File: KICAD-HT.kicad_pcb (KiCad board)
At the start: 4 copper layers, 85 x 70 mm, 147 parts, among them J1 HV_BIAS_IN, J2 DC_HT, Q1 IPD050N10N5, Q2 IPD050N10N5, Q4 MMBF170, Q5 IPD60R360P7, Q6 BSS127I, Q7 BSS127I, T1 MSD1514-103ME, U1 UCC27517, U10 ISO7710, U11 AMC0311R, U12 UCC24612, U13 SN74LVC1G08, U14 TSV791, U15 ATL431, U16 LMV7219, U17 SN74LVC1G132, U18 SN74LVC1G74, U19 ISO7710F, U20 VODA1275, U21 MCP6001, U22 AMC0302R, U3 ISO7710, U5 DPC817, U7 AMC0311R, U9 AMC0302R

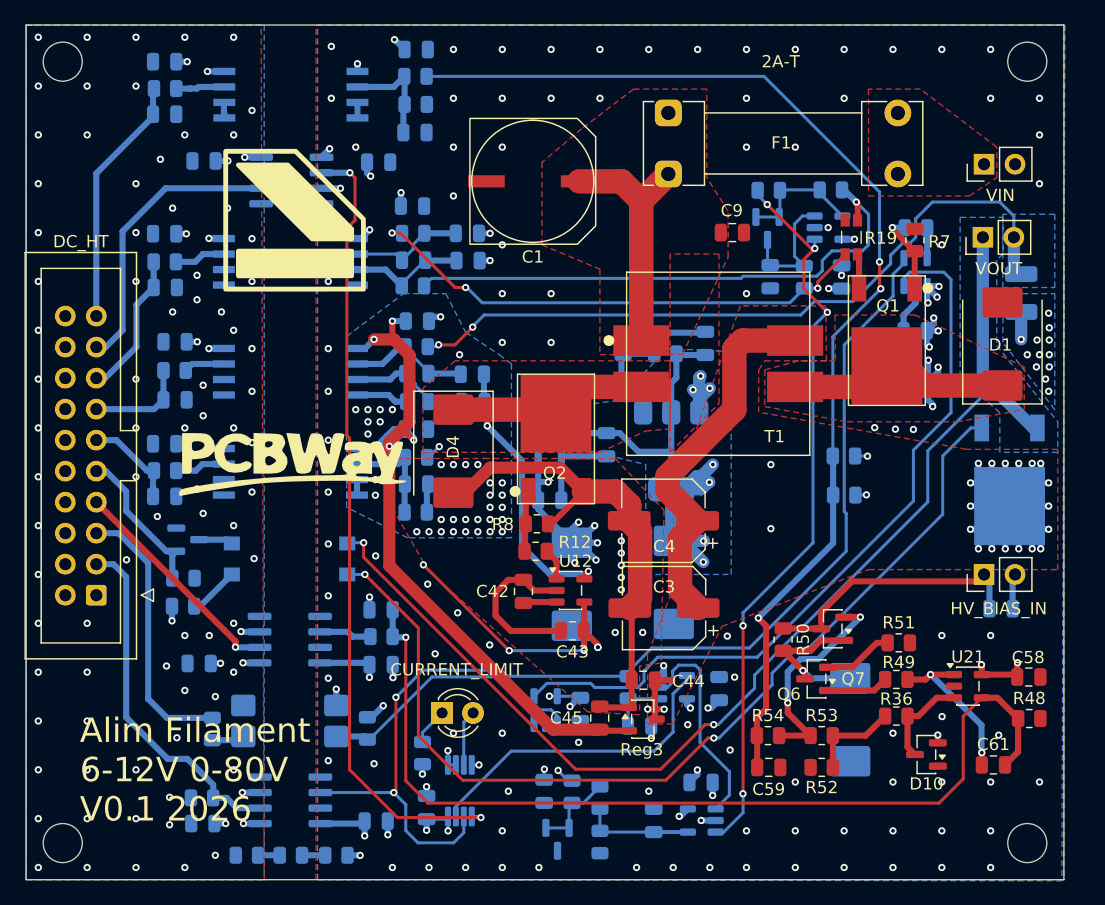
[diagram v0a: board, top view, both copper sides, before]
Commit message: Nettoie les 3 dernieres violations hors silkscreen : exclut les broches NC de barriere_controle (U19 pin7), force la connexion solide aux pastilles GND/VOUT_N starved_thermal (C18/U14/C55/C51)
Co-Authored-By: Claude Sonnet 5 <noreply@anthropic.com>
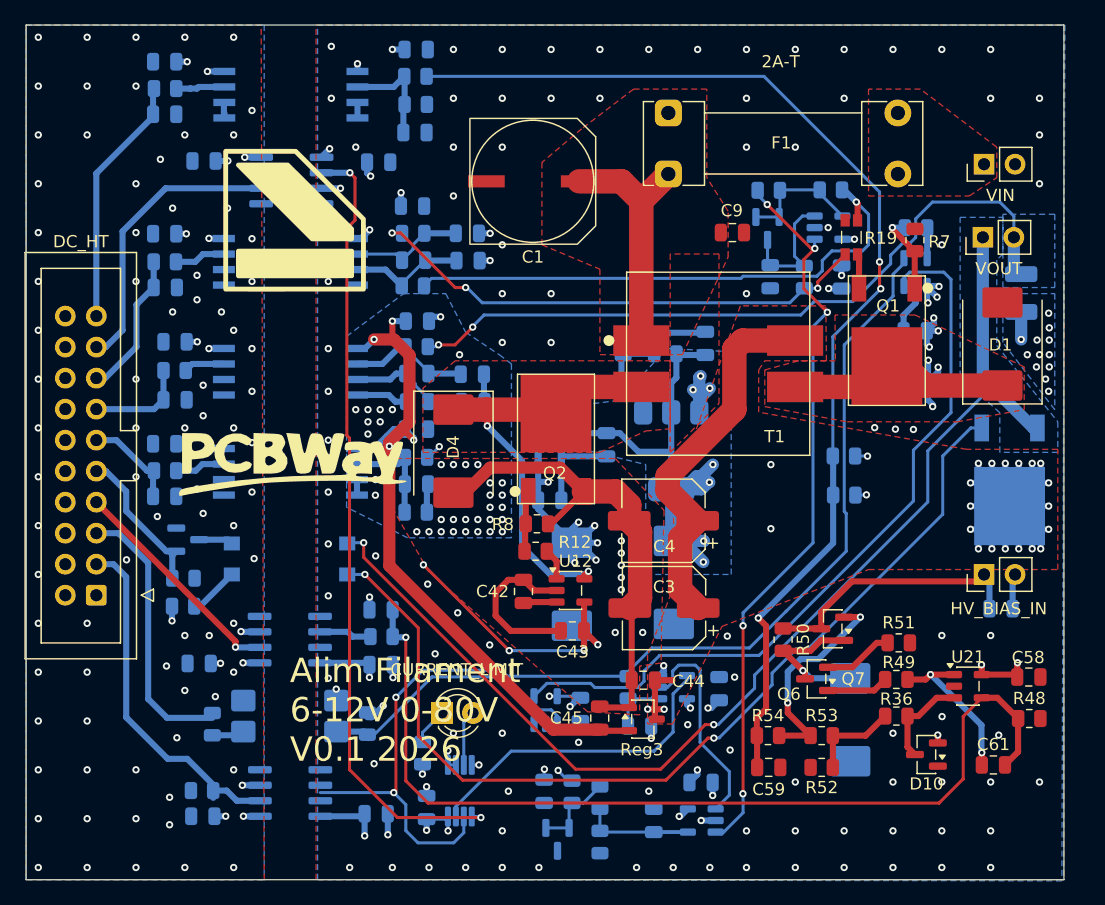
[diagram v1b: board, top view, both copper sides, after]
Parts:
- removed R37, R38, R39: 1M, Resistor_SMD:R_0805_2012Metric
- removed REF** (x4): MountingHole_3.2mm_M3, MountingHole:MountingHole_3.2mm_M3
- moved C15 0.60 mm to (109.5, 111.8)
- moved C16 0.60 mm to (123.7, 111.6)
- moved R5 0.60 mm to (109.4, 109.7)
- moved U3 0.60 mm to (116.6, 109.9)
- moved U5 0.40 mm to (116.6, 103.6)
- moved R3 0.40 mm to (110.3, 104.3)
- moved R4 0.40 mm to (123.0, 104.2)
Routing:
- net Net-(R38-Pad1): track 1.90 -> 0.00 mm
- net Net-(R37-Pad1): track 1.78 -> 0.00 mm
- net GND: track 43.3 -> 42.3 mm, vias 114 -> 113
- net VOUT_P: track 84.6 -> 84.4 mm, vias 27 -> 26

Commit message: Corrige silk_over_copper Q1/Q2/Q5/T1/C1 et ajoute VODA1275 a fp-lib-table
Repercute dans les empreintes placees (copies embarquees du .kicad_pcb)
la correction de contour apportee a TO252-3_TabPin2/MSD1514/A786MW_VChip
dans lib_fp_commun -- KiCad ne resynchronise pas automatiquement une
empreinte placee quand le fichier librairie change, il fallait editer
les deux. Ajoute aussi l'entree VODA1275 manquante dans fp-lib-table
(bibliotheque presente sur disque et deja utilisee par U20, jamais
enregistree ici -- presente dans KICAD-HV, oubliee ici).

41 -> 23 avertissements DRC (0 regression verifiee par diff avant/apres).

Co-Authored-By: Claude Sonnet 5 <noreply@anthropic.com>
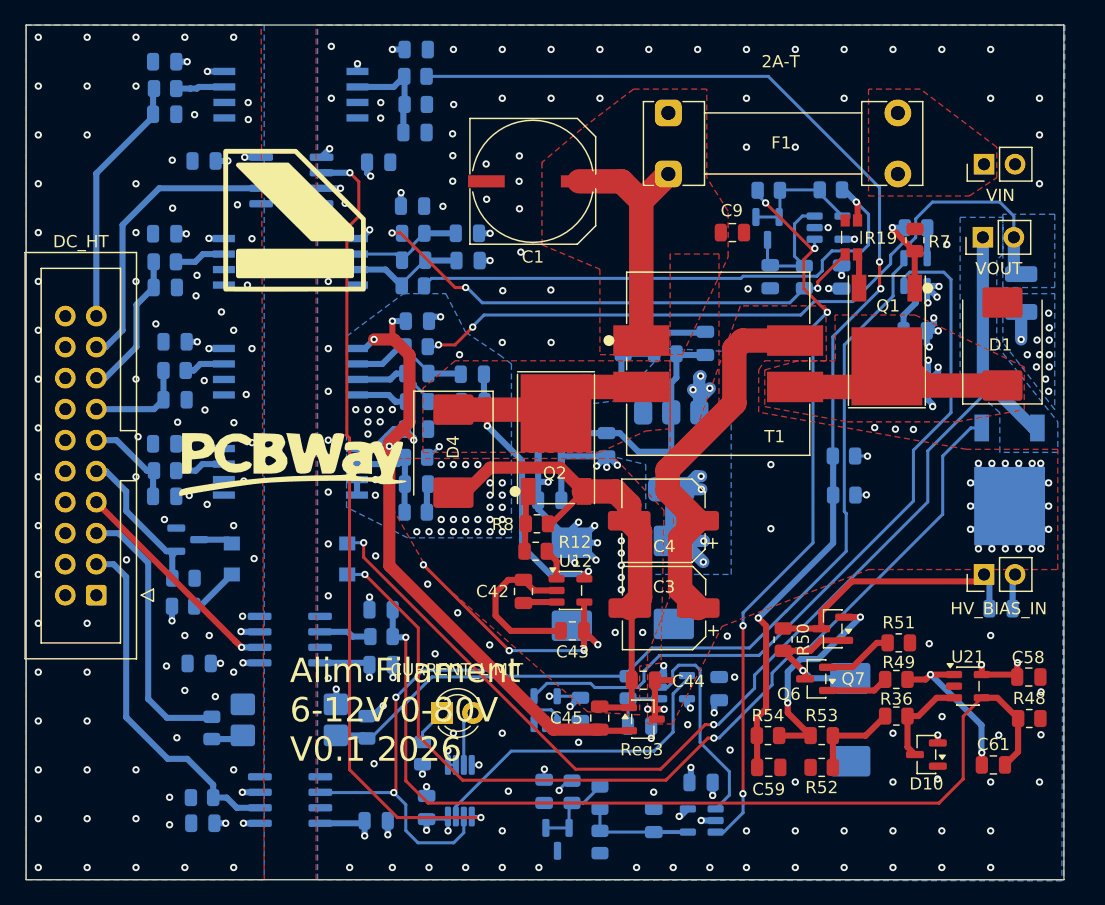
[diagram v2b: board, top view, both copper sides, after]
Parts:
- moved C15 0.58 mm to (109.5, 112.4)
- moved C16 0.58 mm to (123.7, 112.2)
- moved R5 0.58 mm to (109.4, 110.3)
- moved U3 0.57 mm to (116.6, 110.5)
- moved R3 0.31 mm to (110.2, 104.6)
- moved U5 0.31 mm to (116.6, 103.9)
- moved R4 0.31 mm to (122.9, 104.5)
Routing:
- net RAIL_8V25: track 55.1 -> 52.9 mm
- net GND: track 42.3 -> 44.2 mm, vias 113 -> 126
- net GND_CTRL: track 1.30 -> 0.00 mm

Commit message: Corrige le sliver VOUT_N/GND, remet les trous de fixation, fixe le 3D de F1
Travail de nettoyage silkscreen (texte titre, champs reference, J2) et
contour de zone (pointe de cuivre VOUT_N pres du via RAIL_8V25, decouverte
via reconstruction geometrique des zones remplies faute de coordonnees
dans le rapport DRC). Modele 3D de F1 repointe vers
Fuseholder_Cylinder-5x20mm_Schurter_0031_8201_Horizontal_Open.step
(echelle 0.836 pour coller au pas 18.8mm existant) -- le fichier original
Littelfuse_111_Lateral n'a jamais existe dans la bibliotheque 3D KiCad
stock (verifie sur le depot officiel), aucune pastille ni routage touche.

DRC propre (0 violation).

Co-Authored-By: Claude Sonnet 5 <noreply@anthropic.com>
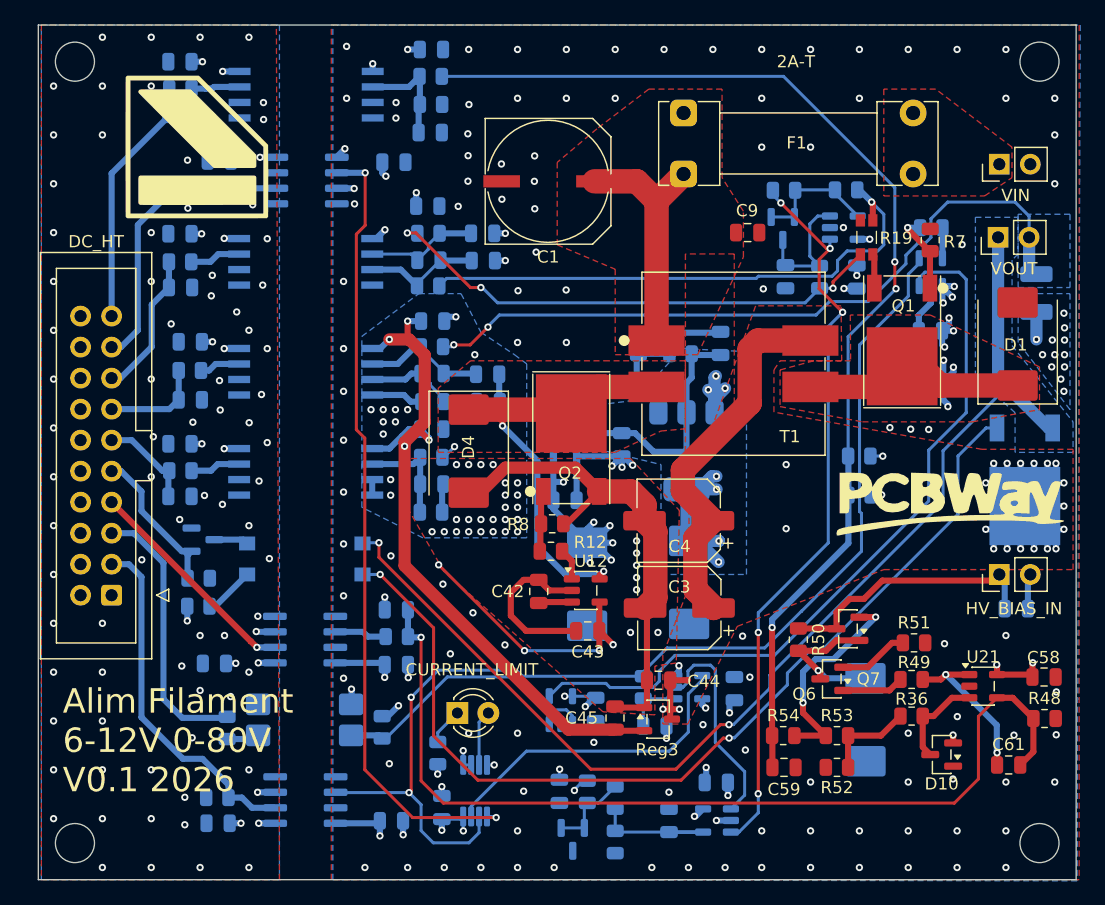
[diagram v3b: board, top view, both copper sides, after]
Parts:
- added H1: MountingScrew, MountingHole:MountingHole_3.2mm_M3, F.Cu at (99.0, 50.0)
- added H2: MountingScrew, MountingHole:MountingHole_3.2mm_M3, F.Cu at (99.0, 114.0)
- added H3: MountingScrew, MountingHole:MountingHole_3.2mm_M3, F.Cu at (178.0, 114.0)
- added H4: MountingScrew, MountingHole:MountingHole_3.2mm_M3, F.Cu at (178.0, 50.0)
- moved G*** 53.9 mm to (171.0, 86.0)
- moved G*** 10.0 mm to (109.0, 57.0)
- moved C37 1.25 mm to (128.3, 71.2)
- moved R40 1.25 mm to (128.2, 73.3)
- moved C1 1.25 mm to (137.8, 59.8)
- moved C10 1.25 mm to (151.9, 73.1)
- moved C13 1.25 mm to (143.8, 81.4)
- moved C14 1.25 mm to (139.1, 85.9)
- moved C15 1.25 mm to (110.7, 112.4)
- moved C16 1.25 mm to (124.9, 112.2)
- moved C18 1.25 mm to (128.2, 80.1)
- moved C19 1.25 mm to (169.1, 72.0)
- moved C21 1.25 mm to (169.2, 76.2)
- moved C23 1.25 mm to (128.2, 84.6)
- moved C24 1.25 mm to (107.6, 85.6)
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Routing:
- net HV_BIAS_OUT: track 93.2 -> 92.6 mm
- net GND_CTRL: vias 80 -> 78

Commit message: Finalise la regle HT_distance_90V (HV_BIAS_OUT trace, starved_thermal C37)
Passes successives de reduction des faux positifs par tracage reel du
circuit (pas par le nom des nets) :
- HV_BIAS_OUT ajoute cote A (pas exclu) : verifie pilote activement par
  la boucle de linearisation (Q7/MCP6001) et couple a VOUT_P/VOUT_N par
  le pont 2x100kOhm R9/R10 -- atteint reellement ~90V, contrairement a
  l'hypothese initiale qui l'avait classe "meme domaine, sans danger".
- HV_BIAS_IN (J1) verifie et laisse hors de la classe SEC : decouple
  vers le vrai GND (C62, J1 broche 2), entree brute avant regulation,
  domaine different malgre le nom proche de HV_BIAS_OUT.
- Net-(U22-INP)/Net-(U22-INN)/ISNS_P ajoutes a la netclasse SEC
  (KICAD-HT.kicad_pro) : U22 (AMC0302R) a sa broche GND1 litteralement
  sur VOUT_N, ISNS_P relie a Net-(U22-INP) via R40 -- meme domaine.
- Exemptions nominative R9, R10, R54 (pastille-contre-pastille-du-
  meme-composant, zone au lieu de pad -- meme motif que T1, cas que
  A.Parent ne couvre pas pour une zone).

DRC propre : 0 violation, 0 element non connecte. Inclut aussi la
correction starved_thermal de C37 (connexion directe a la zone VOUT_N,
pastille trop petite pour 2 rayons de frein thermique).

Co-Authored-By: Claude Sonnet 5 <noreply@anthropic.com>
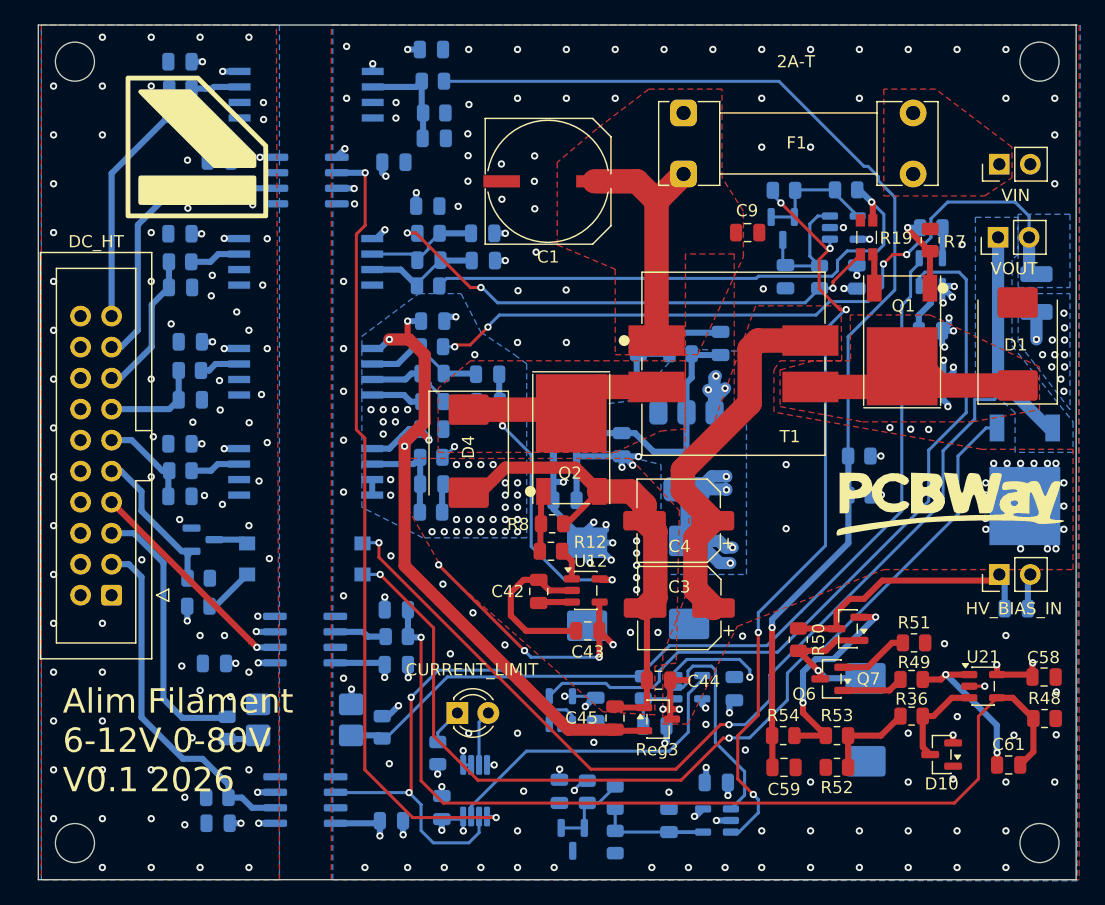
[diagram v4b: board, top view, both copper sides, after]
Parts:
- moved R23 0.74 mm to (128.4, 54.2)
- moved C40 0.58 mm to (128.4, 56.3)
- moved R22 0.43 mm to (128.3, 51.6)
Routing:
- net GND: track 44.2 -> 53.1 mm, vias 126 -> 125
- net VOUT_P: track 84.4 -> 91.3 mm, vias 26 -> 25
- net RAIL_8V25: track 52.9 -> 56.9 mm
- net ISNS_AMP: track 60.8 -> 62.8 mm
- net V_HT_OUT: track 95.7 -> 97.2 mm
- net SW_SEC: track 36.0 -> 37.4 mm
- net ISNS_P: track 62.5 -> 63.4 mm, vias 2 -> 4
- net U15_OUTP: track 79.4 -> 80.2 mm
- net HV_BIAS_OUT: track 92.6 -> 91.9 mm, vias 3 -> 1

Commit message: Vias thermiques sous Q1 (SW_PRI) et Q2 (SW_SEC) + reduction In2.Cu
Q1 : 15 vias (grille 3x5, pas 1,1mm) sous le tab, zone SW_PRI sur B.Cu
ajoutee par l'utilisateur pour etaler la chaleur -- secteur contraint
par du routage GND/RAIL_8V25/PWM_PRI_OUT existant sous le tab, filtre
obstacle par obstacle (shapely) avant pose. 9 vias testes a pas 1,0mm
plus pres de C19/C21 retires : ils cassaient leur connexion GND
(starved_thermal + pastille non connectee).

Q2 : 25 vias (grille complete 5x5, pas 1,1mm) sous le tab, secteur
beaucoup moins charge -- aucun obstacle n'a bloque de candidat. Zone
SW_SEC sur B.Cu deja posee par l'utilisateur.

In2.Cu : zones reduites par l'utilisateur (le plan reste decoupe en
plusieurs rails, accepte en l'etat -- faible courant attendu sur
RAIL_3V3_PRI, cf. revue de ce soir).

DRC propre : 0 violation sur l'etat final.

Co-Authored-By: Claude Sonnet 5 <noreply@anthropic.com>
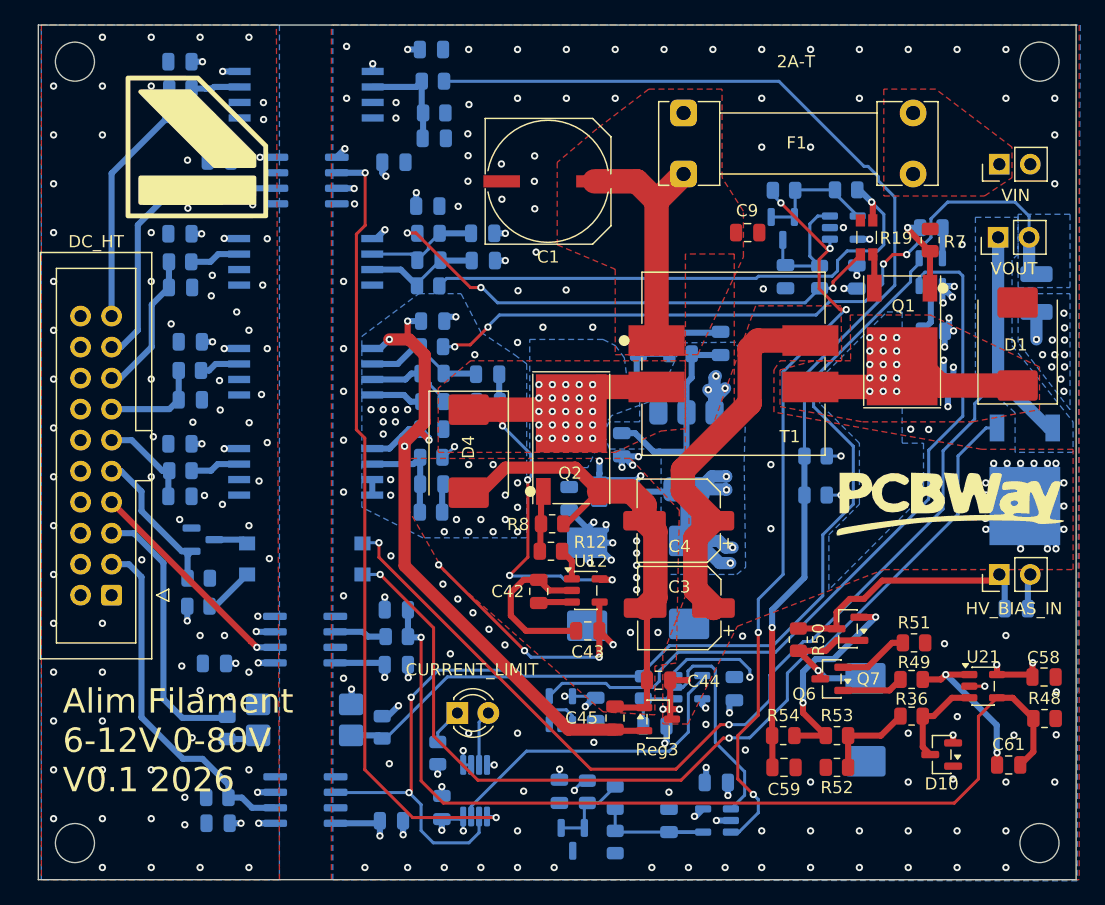
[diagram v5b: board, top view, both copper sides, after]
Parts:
- moved Reg2 5.57 mm to (143.1, 85.2), turned to 0 degrees
- moved R10 3.60 mm to (159.7, 85.5)
- moved R9 3.58 mm to (159.7, 82.3)
- moved C21 0.42 mm to (169.6, 76.2)
- moved C14 0.37 mm to (139.5, 85.8), turned to 90 degrees
- moved C19 0.24 mm to (169.3, 72.1)
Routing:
- net GND: track 53.1 -> 41.5 mm, vias 125 -> 127
- net VOUT_P: track 91.3 -> 84.9 mm
- net SW_SEC: track 37.4 -> 41.4 mm, vias 2 -> 29
- net PWM_PRI_OUT: track 92.7 -> 95.6 mm
- net RAIL_3V3_PRI: track 61.5 -> 59.8 mm, vias 31 -> 32
- net V_HT_OUT: track 97.2 -> 96.3 mm
- net VOUT_N: track 68.2 -> 68.5 mm, vias 55 -> 43
- net SW_PRI: vias 0 -> 15
- added copper zone on B.Cu, net SW_PRI
- added copper zone on B.Cu, net SW_SEC
